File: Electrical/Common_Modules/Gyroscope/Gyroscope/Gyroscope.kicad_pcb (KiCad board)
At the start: 2 copper layers, 30 x 22.9 mm, 5 parts, among them IC101 BMI088, J101 Conn_01x08, J102 Conn_01x08

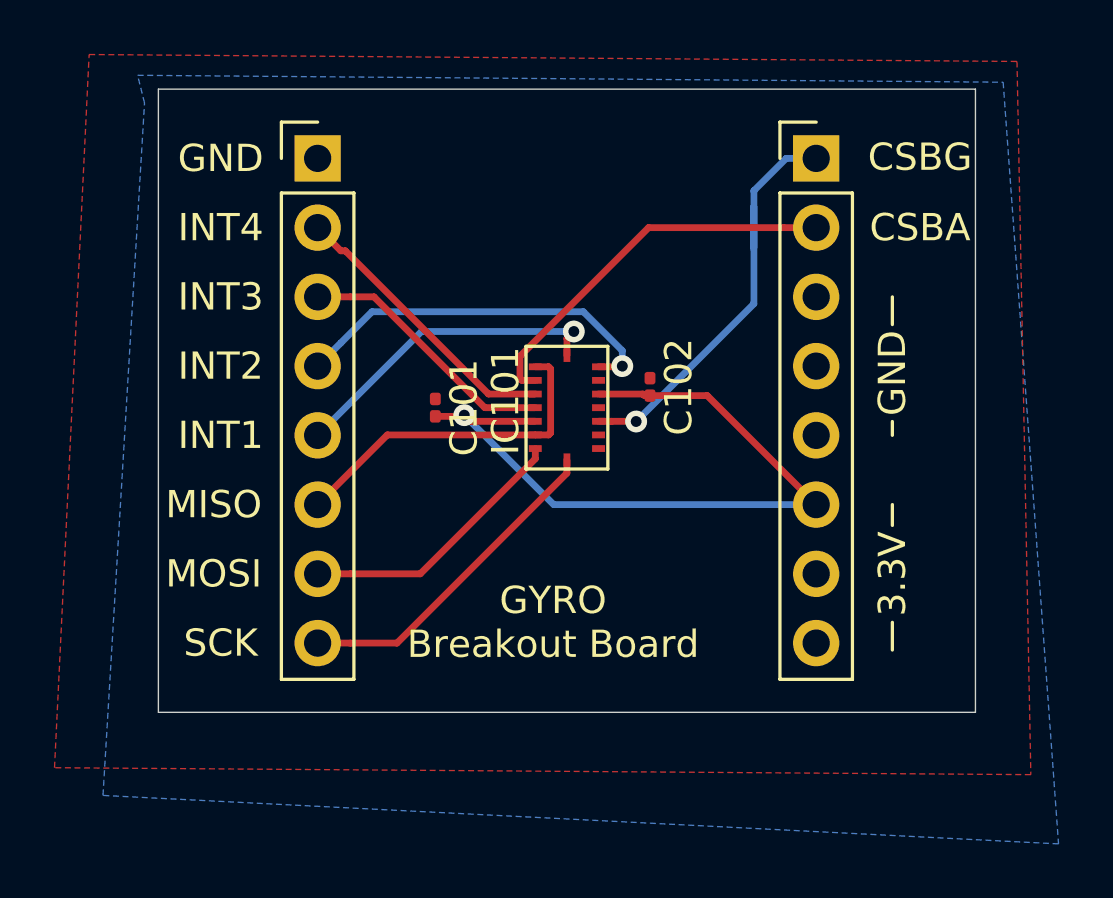
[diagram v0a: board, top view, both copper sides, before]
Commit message: Double check the design rule checker to make sure all your pins are hooked up
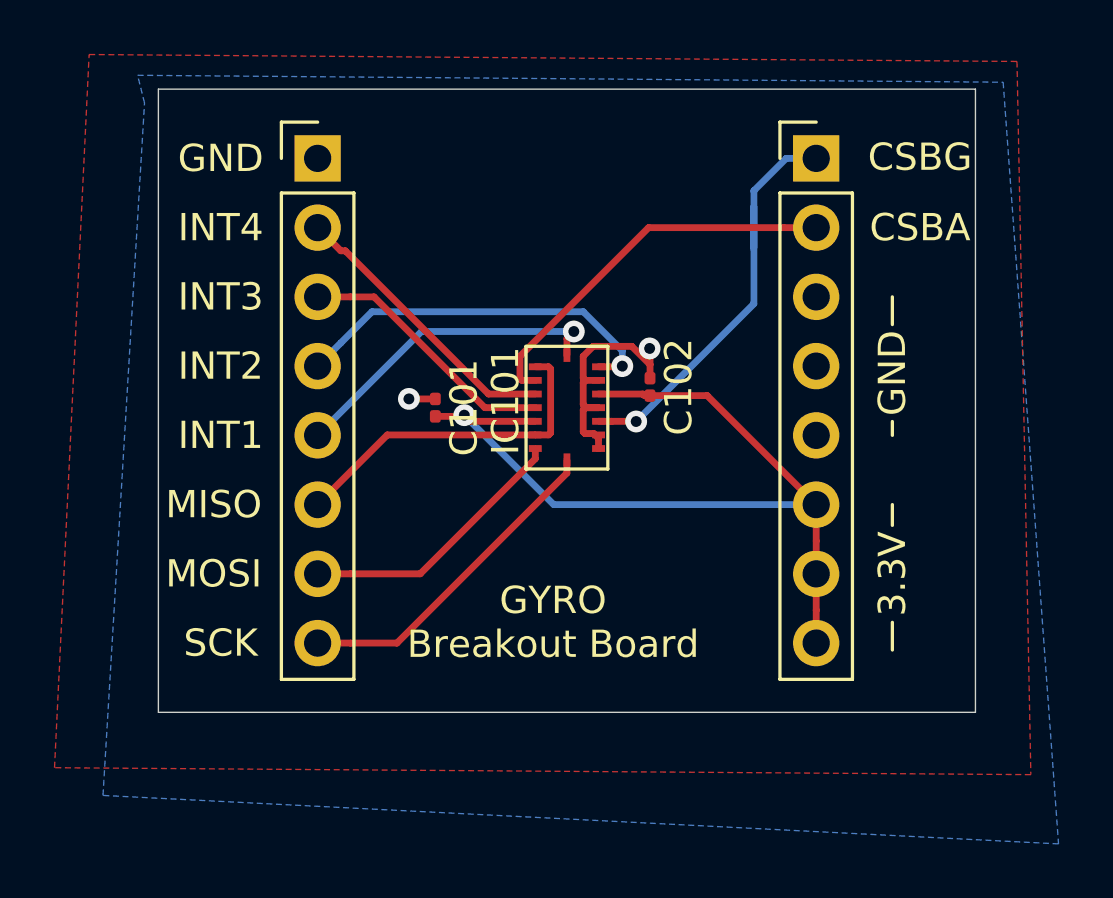
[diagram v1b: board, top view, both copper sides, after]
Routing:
- net GND: track 0.00 -> 10.3 mm, vias 0 -> 2
- net +3V3: track 27.7 -> 32.8 mm
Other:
- net class Default: clearance 0.2 -> 0.1524
- rule trace_clearance: 0.2 -> 0.1524
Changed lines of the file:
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@@
     (thickness 1.6)
     (drawings 21)
-    (tracks 64)
+    (tracks 92)
     (zones 0)
     (modules 5)
@@
   (setup
     (last_trace_width 0.25)
-    (trace_clearance 0.2)
+    (trace_clearance 0.1524)
     (zone_clearance 0.508)
     (zone_45_only no)
@@
     (solder_mask_min_width 0.25)
     (aux_axis_origin 0 0)
-    (visible_elements FFFFFF7F)
+    (visible_elements 7FFFFFFF)
     (pcbplotparams
       (layerselection 0x010fc_ffffffff)
@@
   (net 11 /INT1_ACCEL)
   (net_class Default "This is the default net class."
-    (clearance 0.2)
+    (clearance 0.1524)
     (trace_width 0.25)
     (via_dia 0.8)
@@
   (gr_line (start 113.03 107.188) (end 113.03 84.328) (layer Edge.Cuts) (width 0.05))
   (gr_line (start 143.002 107.188) (end 113.03 107.188) (layer Edge.Cuts) (width 0.05))
+  (segment (start 128.6885 96.012) (end 129.176 96.012) (width 0.25) (layer F.Cu) (net 1))
+  (segment (start 128.613499 96.087001) (end 128.6885 96.012) (width 0.25) (layer F.Cu) (net 1))
+  (segment (start 128.613499 96.897001) (end 128.613499 96.087001) (width 0.25) (layer F.Cu) (net 1))
+  (segment (start 128.678508 96.96201) (end 128.613499 96.897001) (width 0.25) (layer F.Cu) (net 1))
+  (segment (start 129.00101 96.96201) (end 128.678508 96.96201) (width 0.25) (layer F.Cu) (net 1))
+  (segment (start 129.176 97.137) (end 129.00101 96.96201) (width 0.25) (layer F.Cu) (net 1))
+  (segment (start 129.176 97.512) (end 129.176 97.137) (width 0.25) (layer F.Cu) (net 1))
+  (segment (start 128.613499 95.087001) (end 128.6885 95.012) (width 0.25) (layer F.Cu) (net 1))
+  (segment (start 128.613499 95.897001) (end 128.613499 95.087001) (width 0.25) (layer F.Cu) (net 1))
+  (segment (start 128.728498 96.012) (end 128.613499 95.897001) (width 0.25) (layer F.Cu) (net 1))
+  (segment (start 129.176 96.012) (end 128.728498 96.012) (width 0.25) (layer F.Cu) (net 1))
+  (segment (start 128.6885 95.012) (end 129.176 95.012) (width 0.25) (layer F.Cu) (net 1))
+  (segment (start 128.613499 94.936999) (end 128.6885 95.012) (width 0.25) (layer F.Cu) (net 1))
+  (segment (start 128.613499 94.126999) (end 128.613499 94.936999) (width 0.25) (layer F.Cu) (net 1))
+  (segment (start 128.977499 93.762999) (end 128.613499 94.126999) (width 0.25) (layer F.Cu) (net 1))
+  (segment (start 130.396001 93.762999) (end 128.977499 93.762999) (width 0.25) (layer F.Cu) (net 1))
+  (segment (start 131.064 94.430998) (end 130.396001 93.762999) (width 0.25) (layer F.Cu) (net 1))
+  (segment (start 131.064 94.93) (end 131.064 94.430998) (width 0.25) (layer F.Cu) (net 1))
+  (segment (start 123.19 95.692) (end 122.222 95.692) (width 0.25) (layer F.Cu) (net 1))
+  (via (at 122.22 95.69) (size 0.8) (drill 0.4) (layers F.Cu B.Cu) (net 1))
+  (segment (start 122.222 95.692) (end 122.22 95.69) (width 0.25) (layer F.Cu) (net 1))
+  (via (at 131.05 93.84) (size 0.8) (drill 0.4) (layers F.Cu B.Cu) (net 1))
+  (segment (start 131.064 94.430998) (end 131.064 93.854) (width 0.25) (layer F.Cu) (net 1))
+  (segment (start 131.064 93.854) (end 131.05 93.84) (width 0.25) (layer F.Cu) (net 1))
   (segment (start 126.856 96.512) (end 124.431 96.512) (width 0.25) (layer F.Cu) (net 2))
   (segment (start 124.251 96.332) (end 123.19 96.332) (width 0.25) (layer F.Cu) (net 2))
@@
   (segment (start 127.532 99.568) (end 137.16 99.568) (width 0.25) (layer B.Cu) (net 2))
   (segment (start 124.251 96.287) (end 127.532 99.568) (width 0.25) (layer B.Cu) (net 2))
+  (segment (start 137.16 103.445919) (end 137.16 102.108) (width 0.25) (layer F.Cu) (net 2))
+  (segment (start 137.16 104.648) (end 137.16 103.445919) (width 0.25) (layer F.Cu) (net 2))
+  (segment (start 137.16 100.905919) (end 137.16 99.568) (width 0.25) (layer F.Cu) (net 2))
+  (segment (start 137.16 102.108) (end 137.16 100.905919) (width 0.25) (layer F.Cu) (net 2))
   (via (at 130.048 94.488) (size 0.8) (drill 0.4) (layers F.Cu B.Cu) (net 3))
   (segment (start 129.176 94.512) (end 130.024 94.512) (width 0.25) (layer F.Cu) (net 3))
